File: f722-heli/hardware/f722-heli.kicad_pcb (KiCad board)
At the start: 6 copper layers, 39.2 x 25.4 mm, 156 parts, among them J1 USB4105-GF-A-120, J10 PORT B / JST GH, J11 PORT C / JST GH, J12 DSM / JST ZH, J2 S1 / GND-VX-S, J3 S2 / GND-VX-S, J4 S3 / GND-VX-S, J5 TAIL / GND-VX-S, J6 ESC / GND-VX-S, J7 RPM / GND-VX-S, J8 SBUS / GND-VX-S, J9 PORT A / JST GH, Q1 BSS138LT1G, Q2 BSS138LT1G, SW1 BOOT / KMT031NGJLHS, U1 STM32F722RET6, U10 TPS2553DRVR / USB input limit, U11 TPS2553DRVR / DSM output limit, U12 USBLC6-4SC6 / header clamp, U13 USBLC6-4SC6 / header clamp, U14 TPD4E05U06DQAR / UART ESD, U15 TPD4E05U06DQAR / UART ESD, U16 PESD15VS2UT,215 / 15V ESD, U2 ICM-42688-P, U3 W25N01GVZEIG / 128MiB, U4 DPS368XTSA1 / 0x76, U5 TPS259472ARPWR, U6 TPS63070RNMR / nominal 5.088V, U7 TPS2117DRLR / ABC priority mux, U8 TPS2121RUXR / BEC-priority co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, U9 TPS62162DSGR / 3.3V 1A, Y1 8MHz / CL10pF / TAXM8M4RDBCCT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

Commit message: F722: add final routed PCB and paired schematics
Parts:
- C63, C65, Q2: moved to B.Cu
- C75, D3, D4, R14, R32: moved to F.Cu
- J1: value USB4105-GF-A-120 -> USB4145-03-0170-C; footprint F722_Heli:USB_C_Receptacle_GCT_USB4105-xx-A_16P_TopMnt_Horizontal -> F722_Heli:USB_C_Receptacle_GCT_USB4145-03-0170-C_16P_Vertical
- J2, J3, J4, J5, J6, J7, J8: footprint F722_Heli:Samtec_HTSW-101-08-L-T-RA_TripleRow -> F722_Heli:Samtec_HTSW-101-08-L-T-RA_TripleRow_OpenEdgeSilk
- R16: value 0.15R / 1% / VCAP ESR -> 0.12R / 1% / VCAP ESR; footprint F722_Heli:R_0603_1608Metric -> F722_Heli:R_Panasonic_ERJ3R_0603
- R31: footprint F722_Heli:R_0402_1005Metric -> F722_YAGEO:R_0201_0603Metric_YAGEO_AC; moved to F.Cu
- R5: footprint F722_Heli:R_0402_1005Metric -> F722_Heli:R_0402_1005Metric_R5_ClearPin1Silk
- moved R35 28.5 mm to (33.2, 18.1), turned to 180 degrees
- moved R34 24.3 mm to (29.6, 20.3), turned to 90 degrees
- moved Q2 22.8 mm to (1.95, 14.2), turned to 0 degrees
- moved R56 21.3 mm to (14.8, 3.55), turned to -165 degrees
- moved U12 17.1 mm to (28.9, 17.1), turned to 180 degrees
- moved R31 14.9 mm to (20.7, 9.86), turned to 180 degrees
- moved R30 10.7 mm to (5.60, 0.80), turned to 180 degrees
- moved R32 9.03 mm to (28.0, 12.6)
- moved R61 8.62 mm to (34.3, 7.80)
- moved C75 7.09 mm to (31.4, 13.5), turned to -90 degrees
- moved D6 6.66 mm to (34.5, 9.60), turned to 90 degrees
- moved D4 6.52 mm to (35.0, 12.6), turned to 180 degrees
- moved R69 6.29 mm to (32.3, 9.20), turned to 0 degrees
- moved TP4 6.00 mm to (0.90, 1.90)
- moved D5 5.93 mm to (35.7, 16.4), turned to 90 degrees
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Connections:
- U14 pad 10: unconnected-(U14-NC10-Pad10) -> PORT_A_RX_EXT
- U14 pad 6: unconnected-(U14-NC6-Pad6) -> PORT_B_TX_EXT
- U14 pad 7: unconnected-(U14-NC7-Pad7) -> PORT_B_RX_EXT
- U14 pad 9: unconnected-(U14-NC9-Pad9) -> PORT_A_TX_EXT
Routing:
- net SERVO1_MCU: track 3.09 -> 101.0 mm, vias 1 -> 5
- net TAIL_MCU: track 5.30 -> 101.6 mm, vias 1 -> 7
- net SERVO2_MCU: track 3.64 -> 99.0 mm, vias 1 -> 9
- net SERVO3_MCU: track 5.31 -> 59.1 mm, vias 1 -> 5
- net PORT_A_RX_EXT: track 4.87 -> 52.5 mm, vias 1 -> 5
- net LED_RED_K: track 2.36 -> 42.2 mm, vias 0 -> 5
- net PORT_C_TX_MCU: track 6.93 -> 45.9 mm, vias 1 -> 4
- net SBUS_HV: track 6.03 -> 39.7 mm, vias 0 -> 4
- net RPM_LV: track 1.74 -> 34.8 mm, vias 1 -> 4
- net ABC_PG: track 59.6 -> 27.4 mm, vias 7 -> 5
- net +5V_BEC: track 62.0 -> 32.7 mm, vias 7 -> 5
- net SBUS_LV: track 1.93 -> 26.6 mm, vias 1 -> 2
- net DSM_RX_MCU: track 29.6 -> 53.2 mm, vias 3 -> 5
- net LED_GREEN_K: track 0.96 -> 23.9 mm, vias 0 -> 2
- net +5V_PERIPH: track 22.0 -> 44.0 mm, vias 7 -> 8
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- added copper zone on F.Cu, net GND
- added copper zone on F.Cu, net VX_RAW
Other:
- board size 39.2 x 25.4 mm -> 41.7 x 25.4 mm

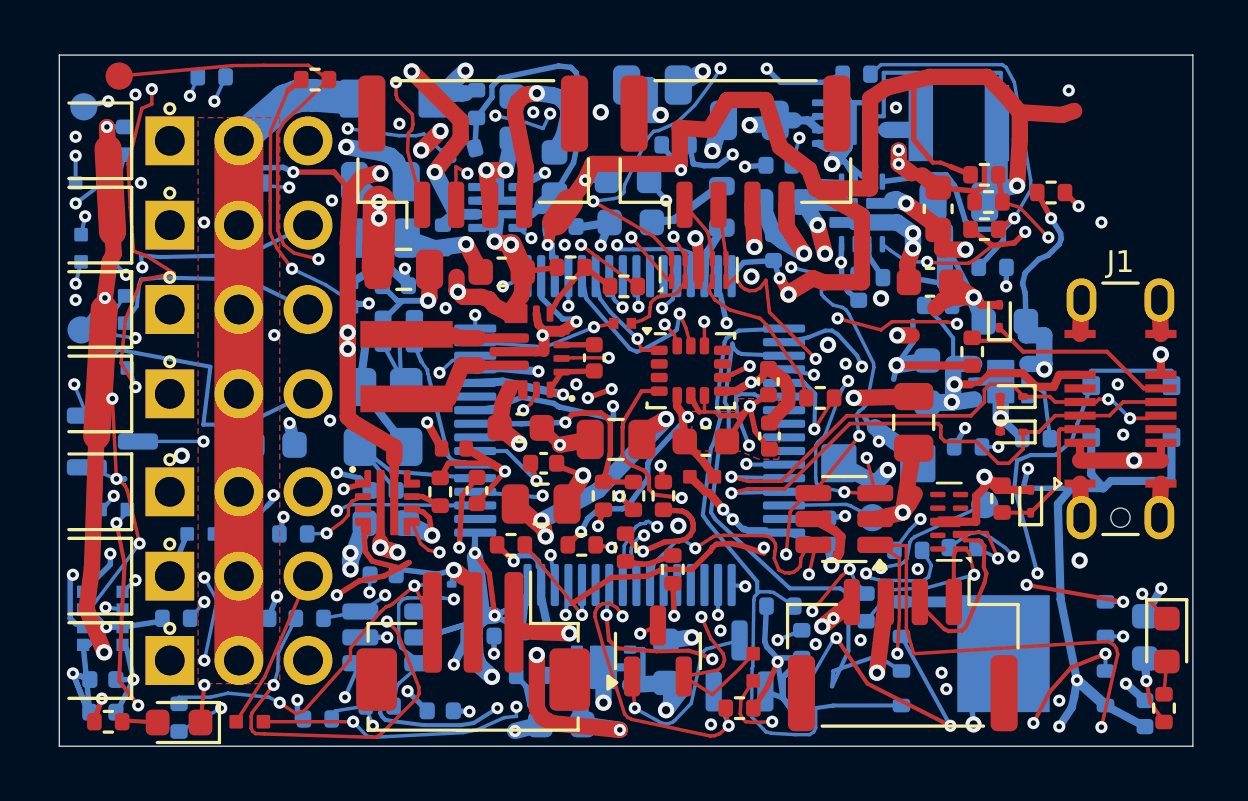
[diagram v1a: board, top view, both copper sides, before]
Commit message: WIP: open the adopted native3 layout from the normal F722 project
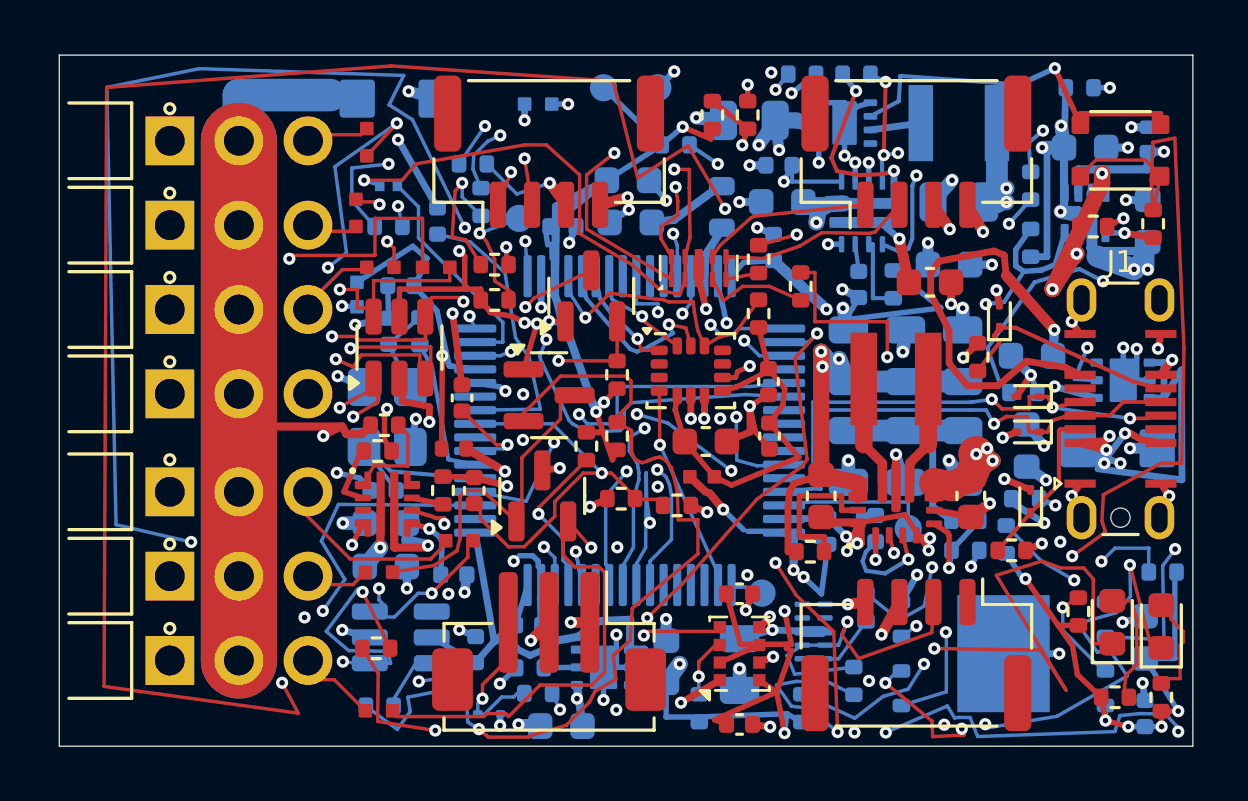
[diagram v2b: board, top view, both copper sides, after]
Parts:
- C16, C17, Q1, Q2, R20, R21, R22, R23, R24, R33, R37, R45, R50, R51, R57, R6, SW1, U4: moved to F.Cu
- C54, C55, C58, C64, C71, C75, R31, R42, R44, R54, R55, R65, TP5, U15: moved to B.Cu
- R7: value 4.7k / 1% -> 2.2k / 1%; moved to F.Cu
- R8: value 4.7k / 1% -> 2.2k / 1%
- moved R10 37.0 mm to (38.8, 23.6)
- moved D1 34.5 mm to (38.7, 20.8), turned to 90 degrees
- moved R8 29.7 mm to (23.5, 24.0), turned to 90 degrees
- moved R2 26.4 mm to (40.2, 6.20), turned to -90 degrees
- moved C60 26.1 mm to (40.0, 3.10), turned to 90 degrees
- moved R57 24.7 mm to (27.6, 18.2)
- moved C17 23.8 mm to (25.0, 19.8)
- moved C61 23.7 mm to (40.0, 6.10)
- moved C16 23.5 mm to (25.0, 24.6)
- moved U4 23.4 mm to (25.0, 22.0)
- moved C57 22.9 mm to (33.2, 14.8), turned to -90 degrees
- moved R58 22.2 mm to (37.5, 1.20), turned to 0 degrees
- moved C56 21.8 mm to (31.1, 14.8), turned to -90 degrees
- moved U7 21.6 mm to (37.7, 5.80), turned to 90 degrees
- moved R56 21.2 mm to (35.7, 6.90), turned to 90 degrees
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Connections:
- U13 pad 1: ESC_MCU -> SBUS_MCU
- U13 pad 3: RPM_MCU -> ESC_MCU
- U13 pad 6: SBUS_MCU -> RPM_MCU
- U15 pad 10: unconnected-(U15-NC10-Pad10) -> PORT_C_RX_EXT
- U15 pad 9: unconnected-(U15-NC9-Pad9) -> PORT_C_TX_EXT
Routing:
- net +5V_BEC: track 32.7 -> 156.1 mm, vias 5 -> 7
- net DSM_RX_MCU: track 53.2 -> 139.5 mm
- net +3V3_CORE: track 305.4 -> 220.1 mm, vias 34 -> 23
- net SERVO2_MCU: track 99.0 -> 34.5 mm, vias 9 -> 5
- net SBUS_LV: track 26.6 -> 75.9 mm
- net SERVO1_MCU: track 101.0 -> 53.3 mm, vias 5 -> 6
- net LED_GREEN_K: track 23.9 -> 71.4 mm, vias 2 -> 4
- net RPM_MCU: track 17.6 -> 59.4 mm, vias 2 -> 5
- net GND: track 173.5 -> 131.9 mm, vias 70 -> 107
- net VX_RAW: track 69.1 -> 110.2 mm, vias 6 -> 3
- net SERVO3_MCU: track 59.1 -> 21.7 mm, vias 5 -> 4
- net FLASH_SCK: track 18.5 -> 49.7 mm, vias 2 -> 5
- net +5V_PERIPH: track 44.0 -> 75.3 mm, vias 8 -> 6
- net USB_ILIM: track 2.45 -> 31.9 mm, vias 0 -> 2
- net PORT_B_RX_MCU: track 3.98 -> 29.6 mm, vias 1 -> 2
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- removed copper zone on In3.Cu, net +5V_PERIPH
- removed copper zone on F.Cu, net GND
- removed copper zone on F.Cu, net VX_RAW

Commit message: WIP: promote the native2 In4 RX prototype baseline with current DC evidence
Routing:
- net PORT_C_RX_MCU: track 5.65 -> 27.1 mm
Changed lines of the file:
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@@
+	)
+	(segment
+		(start 22.408238 13.54364)
+		(end 25.290083 17.120649)
+		(width 0.127)
+		(layer "In4.Cu")
+		(net "PORT_C_RX_MCU")
+	)
+	(segment
+		(start 26.646487 19.288931)
+		(end 27.925338 20.183455)
+		(width 0.127)
+		(layer "In4.Cu")
+		(net "PORT_C_RX_MCU")
+	)
+	(segment
+		(start 27.925338 20.183455)
+		(end 29.494213 19.508784)
+		(width 0.127)
+		(layer "In4.Cu")
+		(net "PORT_C_RX_MCU")
+	)
+	(segment
+		(start 22.56 6.563)
+		(end 23.349615 9.563061)
+		(width 0.127)
+		(layer "In4.Cu")
+		(net "PORT_C_RX_MCU")
+	)
+	(segment
+		(start 25.998064 18.982015)
+		(end 26.646487 19.288931)
+		(width 0.127)
+		(layer "In4.Cu")
+		(net "PORT_C_RX_MCU")
+	)
+	(segment
+		(start 32.150734 19.829002)
+		(end 32.077915 18.824034)
+		(width 0.127)
+		(layer "In4.Cu")
+		(net "PORT_C_RX_MCU")
+	)
+	(segment
+		(start 29.494213 19.508784)
+		(end 32.150734 19.829002)
+		(width 0.127)
+		(layer "In4.Cu")
+		(net "PORT_C_RX_MCU")
+	)
+	(segment
+		(start 23.281459 9.672106)
+		(end 22.408238 13.54364)
+		(width 0.127)
+		(layer "In4.Cu")
+		(net "PORT_C_RX_MCU")
+	)
+	(segment
+		(start 23.349615 9.563061)
+		(end 23.281459 9.672106)
+		(width 0.127)
+		(layer "In4.Cu")
+		(net "PORT_C_RX_MCU")
+	)
+	(segment
+		(start 25.290083 17.120649)
+		(end 25.998064 18.982015)
+		(width 0.127)
+		(layer "In4.Cu")
+		(net "PORT_C_RX_MCU")
 	)
 	(segment

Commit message: WIP: close F722 MOSI and preserve the native1 prototype baseline
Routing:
- net FLASH_MOSI: track 0.00 -> 48.1 mm, vias 0 -> 2
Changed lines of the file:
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@@
 	)
 	(segment
-		(start 19.7 12.35)
-		(end 20 12.325)
+		(start 21.996687 11.652784)
+		(end 24.865539 10.153233)
 		(width 0.127)
 		(layer "In2.Cu")
@@
 	)
 	(segment
-		(start 20 12.325)
-		(end 24.865539 10.153233)
+		(start 19.7 12.35)
+		(end 20 12.325)
 		(width 0.127)
 		(layer "In2.Cu")
@@
 	)
 	(segment
+		(start 20.809576 12.182659)
+		(end 21.996687 11.652784)
+		(width 0.127)
+		(layer "In2.Cu")
+		(net "PORT_B_RX_MCU")
+	)
+	(segment
+		(start 20 12.325)
+		(end 20.809576 12.182659)
+		(width 0.127)
+		(layer "In2.Cu")
+		(net "PORT_B_RX_MCU")
+	)
+	(segment
 		(start 24.865539 10.153233)
 		(end 25.176006 9.934419)
@@
 		(net "FLASH_WP_N")
 	)
+	(via
+		(at 39.500783 16.168262)
+		(size 0.45)
+		(drill 0.2)
+		(layers "F.Cu" "B.Cu")
+		(tenting
+			(front yes)
+			(back yes)
+		)
+		(net "FLASH_MOSI")
+	)
+	(via
+		(at 21.222599 11.513264)
+		(size 0.45)
+		(drill 0.2)
+		(layers "F.Cu" "B.Cu")
+		(tenting
+			(front yes)
+			(back yes)
+		)
+		(net "FLASH_MOSI")
+	)
+	(segment
+		(start 38.45 20.095)
+		(end 37.75 19.4)
+		(width 0.127)
+		(layer "B.Cu")
+		(net "FLASH_MOSI")
+	)
+	(segment
+		(start 26.634999 11.55)
+		(end 25.712467 11.751146)
+		(width 0.127)
+		(layer "B.Cu")
+		(net "FLASH_MOSI")
+	)
+	(segment
+		(start 25.45 11.89)
+		(end 21.222599 11.513264)
+		(width 0.127)
+		(layer "B.Cu")
+		(net "FLASH_MOSI")
+	)
+	(segment
+		(start 37.8 18.05)
+		(end 38.25 17.7)
+		(width 0.127)
+		(layer "B.Cu")
+		(net "FLASH_MOSI")
+	)
+	(segment
+		(start 39.68 17.7)
+		(end 39.68 16.55)
+		(width 0.127)
+		(layer "B.Cu")
+		(net "FLASH_MOSI")
+	)
+	(segment
+		(start 37.75 19.4)
+		(end 37.8 18.05)
+		(width 0.127)
+		(layer "B.Cu")
+		(net "FLASH_MOSI")
+	)
+	(segment
+		(start 39.68 16.55)
+		(end 39.500783 16.168262)
+		(width 0.127)
+		(layer "B.Cu")
+		(net "FLASH_MOSI")
+	)
+	(segment
+		(start 38.25 17.7)
+		(end 39.68 17.7)
+		(width 0.127)
+		(layer "B.Cu")
+		(net "FLASH_MOSI")
+	)
+	(segment
+		(start 25.712467 11.751146)
+		(end 25.45 11.89)
+		(width 0.127)
+		(layer "B.Cu")
+		(net "FLASH_MOSI")
+	)
+	(segment
+		(start 31.009991 20.145995)
+		(end 33.419247 20.062)
+		(width 0.127)
+		(layer "In4.Cu")
+		(net "FLASH_MOSI")
+	)
+	(segment
+		(start 20.045349 23.062343)
+		(end 21.592203 24.588035)
+		(width 0.127)
+		(layer "In4.Cu")
+		(net "FLASH_MOSI")
+	)
+	(segment
+		(start 36.470332 16.044572)
+		(end 37.902703 15.496255)
+		(width 0.127)
+		(layer "In4.Cu")
+		(net "FLASH_MOSI")
+	)
+	(segment
+		(start 21.222599 11.513264)
+		(end 19.155621 15.3)
+		(width 0.127)
+		(layer "In4.Cu")
+		(net "FLASH_MOSI")
+	)
+	(segment
+		(start 18.815707 17.214299)
+		(end 20.062159 17.90883)
+		(width 0.127)
+		(layer "In4.Cu")
+		(net "FLASH_MOSI")
+	)
+	(segment
+		(start 19.155621 15.3)
+		(end 19.155621 16.3)
+		(width 0.127)
+		(layer "In4.Cu")
+		(net "FLASH_MOSI")
+	)
+	(segment
+		(start 22.579304 24.790292)
+		(end 25.154395 24.583833)
+		(width 0.127)
+		(layer "In4.Cu")
+		(net "FLASH_MOSI")
+	)
+	(segment
+		(start 21.592203 24.588035)
+		(end 22.579304 24.790292)
+		(width 0.127)
+		(layer "In4.Cu")
+		(net "FLASH_MOSI")
+	)
+	(segment
+		(start 37.902703 15.496255)
+		(end 39.500783 16.168262)
+		(width 0.127)
+		(layer "In4.Cu")
+		(net "FLASH_MOSI")
+	)
+	(segment
+		(start 25.154395 24.583833)
+		(end 31.009991 20.145995)
+		(width 0.127)
+		(layer "In4.Cu")
+		(net "FLASH_MOSI")
+	)
+	(segment
+		(start 19.155621 16.3)
+		(end 18.815707 17.214299)
+		(width 0.127)
+		(layer "In4.Cu")
+		(net "FLASH_MOSI")
+	)
+	(segment
+		(start 33.419247 20.062)
+		(end 36.470332 16.044572)
+		(width 0.127)
+		(layer "In4.Cu")
+		(net "FLASH_MOSI")
+	)
+	(segment
+		(start 20.062159 17.90883)
+		(end 20.045349 23.062343)
+		(width 0.127)
+		(layer "In4.Cu")
+		(net "FLASH_MOSI")
+	)
 	(segment

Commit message: WIP: preserve the fully routed F722 native0 geometric milestone
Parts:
- moved R35 0.90 mm to (29.2, 23.9), turned to 180 degrees
- moved U15 0.72 mm to (27.7, 21.9), turned to 90 degrees
- moved R34 0.33 mm to (29.6, 20.0)
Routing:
- net PORT_C_RX_EXT: track 3.04 -> 9.03 mm, vias 0 -> 1
- net PORT_C_TX_EXT: track 11.4 -> 9.28 mm
- net FLASH_MISO: track 47.1 -> 49.1 mm
- net GND: track 131.9 -> 133.4 mm
- net FLASH_WP_N: track 7.59 -> 8.28 mm
- net LED_GREEN_K: track 71.4 -> 70.8 mm
- net FLASH_MOSI: track 48.1 -> 48.6 mm

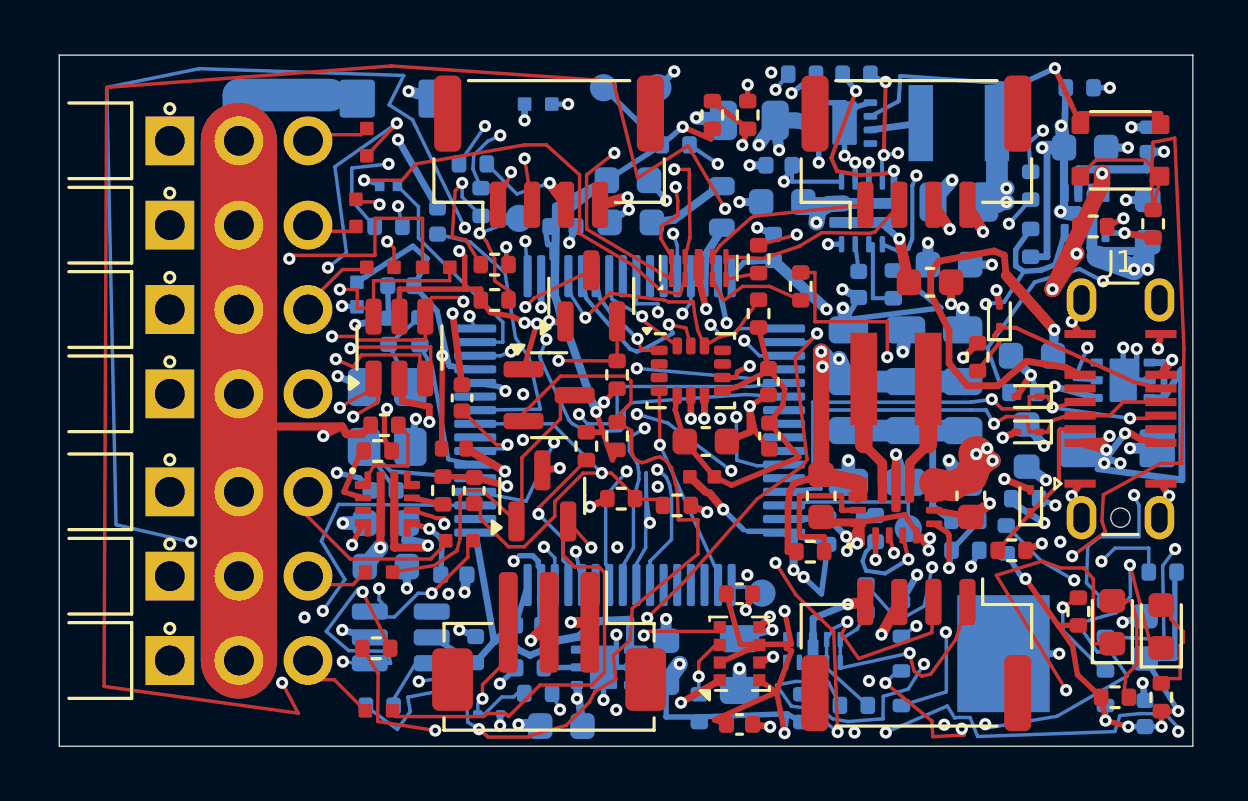
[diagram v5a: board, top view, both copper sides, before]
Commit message: cleaned up nets and added nexus style fc
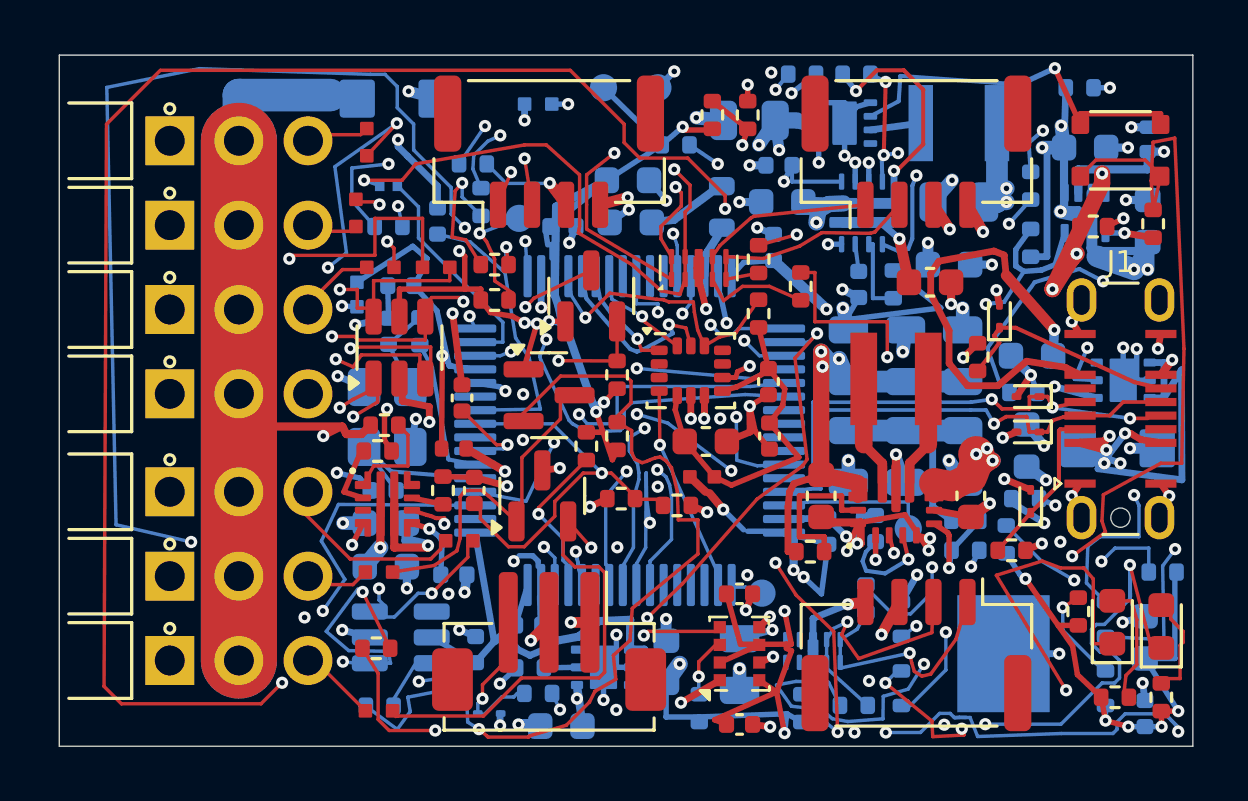
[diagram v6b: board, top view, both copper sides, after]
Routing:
- net DSM_RX_MCU: track 139.5 -> 135.9 mm
- net VX_PROTECTED: track 73.2 -> 74.5 mm
- net FLASH_SCK: track 49.7 -> 50.9 mm
- net SBUS_EXT: track 2.10 -> 2.61 mm

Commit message: tidy up the nets
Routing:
- net SERVO1_MCU: track 53.3 -> 49.4 mm
- net +3V3_CORE: track 219.7 -> 223.0 mm
- net USB_VBUS_RAW: track 52.2 -> 50.0 mm
- net CORE_BUCK_IN: track 23.8 -> 23.0 mm
- net FLASH_MOSI: track 48.6 -> 47.9 mm
- net USB_ILIM: track 31.9 -> 31.3 mm

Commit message: clean up nets
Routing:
- net +3V3_ANALOG: track 13.3 -> 10.3 mm
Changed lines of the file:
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@@
 	)
 	(segment
+		(start 15.284999 12.05)
+		(end 16.0982 12.05)
+		(width 0.2)
+		(layer "B.Cu")
+		(net "GND")
+	)
+	(segment
 		(start 39.9 20.625)
 		(end 39.079 20.845)
@@
 	)
 	(segment
-		(start 16.184999 12.19)
-		(end 16.3958 12.3476)
-		(width 0.2)
-		(layer "B.Cu")
-		(net "GND")
-	)
-	(segment
 		(start 26.634999 17.05)
 		(end 28.25 17.02)
@@
 	)
 	(segment
-		(start 15.284999 12.05)
-		(end 16.184999 12.19)
-		(width 0.2)
-		(layer "B.Cu")
-		(net "GND")
-	)
-	(segment
 		(start 27.91 3.25)
 		(end 27.91 3.95)
@@
 	)
 	(segment
+		(start 16.0982 12.05)
+		(end 16.3958 12.3476)
+		(width 0.2)
+		(layer "B.Cu")
+		(net "GND")
+	)
+	(segment
 		(start 28.86 2.5)
 		(end 28.86 3.7)
@@
 	)
 	(segment
-		(start 13.515 7.475)
-		(end 13.29 8)
-		(width 0.2)
-		(layer "B.Cu")
-		(net "+3V3_ANALOG")
-	)
-	(segment
-		(start 10.94 8.35)
-		(end 12.99 7.025)
+		(start 12.493 7.938)
+		(end 13.03 8.475)
 		(width 0.2)
 		(layer "B.Cu")
@@
 	)
 	(segment
-		(start 13.29 8)
-		(end 13.03 8.475)
+		(start 11.352 7.938)
+		(end 12.493 7.938)
 		(width 0.2)
 		(layer "B.Cu")
@@
 	)
 	(segment
-		(start 13.88 9.4)
-		(end 14.33 11.425)
+		(start 13.797 10.772)
+		(end 14.075 11.05)
 		(width 0.2)
 		(layer "B.Cu")
@@
 	)
 	(segment
-		(start 14.33 11.425)
-		(end 15.284999 11.55)
+		(start 13.03 8.475)
+		(end 13.797 9.242)
 		(width 0.2)
 		(layer "B.Cu")
@@
 	)
 	(segment
-		(start 14.375 11.425)
-		(end 14.075 11.05)
+		(start 13.797 9.242)
+		(end 13.797 10.772)
 		(width 0.2)
 		(layer "B.Cu")
@@
 	)
 	(segment
-		(start 13.03 8.475)
-		(end 13.88 9.4)
+		(start 10.94 8.35)
+		(end 11.352 7.938)
 		(width 0.2)
 		(layer "B.Cu")
@@
 	)
 	(segment
-		(start 15.284999 11.55)
-		(end 14.375 11.425)
+		(start 14.575 11.55)
+		(end 15.284999 11.55)
 		(width 0.2)
 		(layer "B.Cu")
@@
 	)
 	(segment
-		(start 12.99 7.025)
-		(end 13.515 7.475)
+		(start 14.075 11.05)
+		(end 14.575 11.55)
 		(width 0.2)
 		(layer "B.Cu")
